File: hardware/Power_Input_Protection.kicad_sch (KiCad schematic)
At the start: 25 parts, among them J1 JST-PH, Q1 AO3401A, U1 TPS562202S, U2 TPS562202S

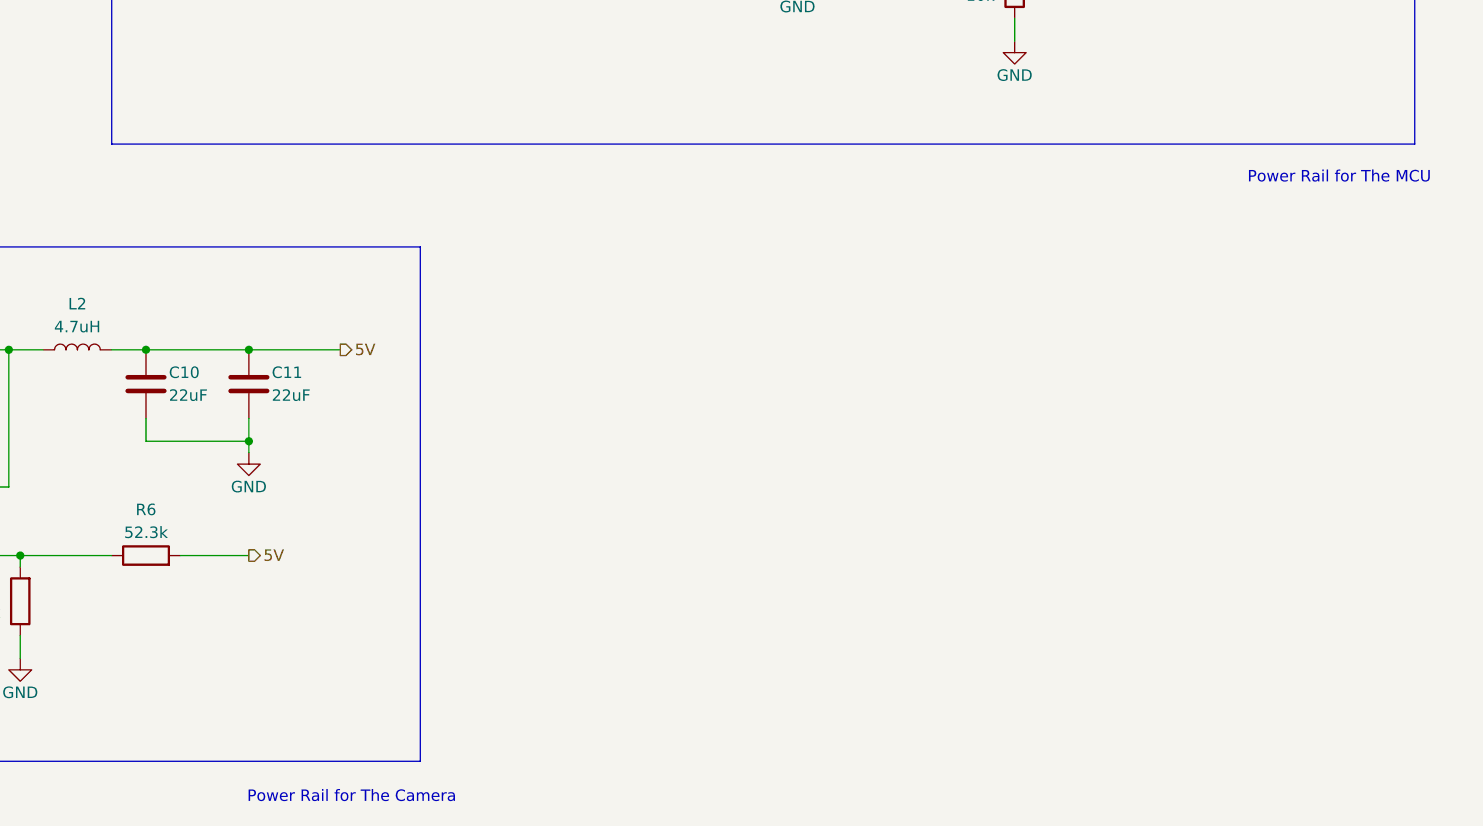
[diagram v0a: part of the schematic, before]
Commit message: Schematic for the MCU and Tag Connect
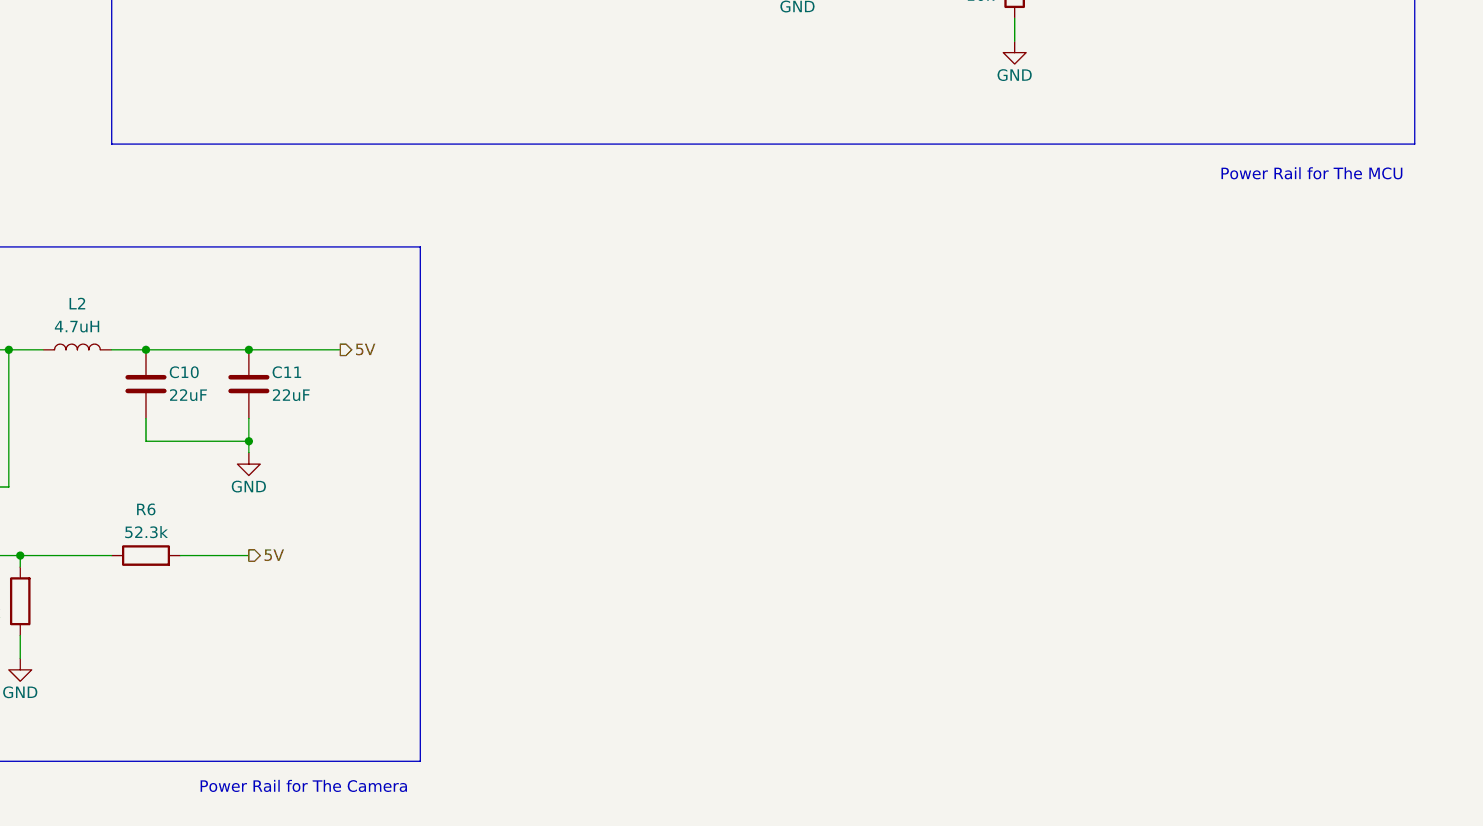
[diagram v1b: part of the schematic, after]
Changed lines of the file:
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@@
 	(text "Power Rail for The Camera\n"
 		(exclude_from_sim no)
-		(at 158.75 181.864 0)
+		(at 153.416 180.848 0)
 		(effects
 			(font
@@
 	(text "Power Rail for The MCU\n"
 		(exclude_from_sim no)
-		(at 268.478 113.03 0)
+		(at 265.43 112.776 0)
 		(effects
 			(font

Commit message: Completed Schematic
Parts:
- added C1: 47uF, symbol Device:C
- renumbered C6 to C10, C12 to C11, C10 to C12, C11 to C13, C1 to C2, C2 to C3, C3 to C4, C7 to C5, C8 to C6, C9 to C7, C4 to C8, C5 to C9, R6 to R4
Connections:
- net GND: now also C1.2
- net VBAT_RAW: now also C1.1
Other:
- moved on the sheet: J1

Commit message: Assigned Footprints and Libraries
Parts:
- C1: footprint (none) -> Capacitor_SMD:C_1210_3225Metric
- C10, C11, C4, C5: footprint (none) -> Capacitor_SMD:C_0603_1608Metric
- C12, C13, C6, C7: footprint (none) -> Capacitor_SMD:C_1206_3216Metric
- C2, C3, C8, C9: footprint (none) -> Capacitor_SMD:C_0805_2012Metric
- F1: footprint (none) -> PMHC_Footprints:F_1812_4532Metric
- J1: footprint (none) -> Connector_JST:JST_PH_S2B-PH-SM4-TB_1x02-1MP_P2.00mm_Horizontal
- L1: footprint (none) -> Inductor_SMD:L_Coilcraft_XFL2010
- L2: footprint (none) -> Inductor_SMD:L_Coilcraft_XAL4020-XXX
- R1, R2, R3, R4, R5: footprint (none) -> Resistor_SMD:R_0201_0603Metric
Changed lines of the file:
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@@
 			)
 		)
-		(property "Footprint" ""
+		(property "Footprint" "Resistor_SMD:R_0201_0603Metric"
 			(at 189.23 89.408 90)
 			(hide yes)
@@
 			)
 		)
-		(property "Footprint" ""
+		(property "Footprint" "Capacitor_SMD:C_1206_3216Metric"
 			(at 148.2852 139.7 0)
 			(hide yes)
@@
 			)
 		)
-		(property "Footprint" ""
+		(property "Footprint" "Capacitor_SMD:C_0805_2012Metric"
 			(at 49.2252 144.78 0)
 			(hide yes)
@@
 			)
 		)
-		(property "Footprint" ""
+		(property "Footprint" "Resistor_SMD:R_0201_0603Metric"
 			(at 234.188 91.44 90)
 			(hide yes)
@@
 			)
 		)
-		(property "Footprint" ""
+		(property "Footprint" "Capacitor_SMD:C_1210_3225Metric"
 			(at 44.1452 53.34 0)
 			(hide yes)
@@
 			)
 		)
-		(property "Footprint" ""
+		(property "Footprint" "Capacitor_SMD:C_1206_3216Metric"
 			(at 136.8552 139.7 0)
 			(hide yes)
@@
 			)
 		)
-		(property "Footprint" ""
+		(property "Footprint" "Capacitor_SMD:C_0805_2012Metric"
 			(at 171.1452 76.2 0)
 			(hide yes)
@@
 			)
 		)
-		(property "Footprint" ""
+		(property "Footprint" "Resistor_SMD:R_0201_0603Metric"
 			(at 135.89 156.718 90)
 			(hide yes)
@@
 			)
 		)
-		(property "Footprint" ""
+		(property "Footprint" "PMHC_Footprints:F_1812_4532Metric"
 			(at 58.42 43.18 0)
 			(hide yes)
@@
 			)
 		)
-		(property "Footprint" ""
+		(property "Footprint" "Resistor_SMD:R_0201_0603Metric"
 			(at 246.38 88.138 90)
 			(hide yes)
@@
 			)
 		)
-		(property "Footprint" ""
+		(property "Footprint" "Resistor_SMD:R_0201_0603Metric"
 			(at 123.698 160.02 90)
 			(hide yes)
@@
 			)
 		)
-		(property "Footprint" ""
+		(property "Footprint" "Inductor_SMD:L_Coilcraft_XFL2010"
 			(at 238.76 63.5 0)
 			(hide yes)
@@
 			)
 		)
-		(property "Footprint" ""
+		(property "Footprint" "Capacitor_SMD:C_1206_3216Metric"
 			(at 258.7752 71.12 0)
 			(hide yes)
@@
 			)
 		)
-		(property "Footprint" ""
+		(property "Footprint" "Capacitor_SMD:C_0603_1608Metric"
 			(at 228.6 77.7748 0)
 			(hide yes)
@@
 			)
 		)
-		(property "Footprint" ""
+		(property "Footprint" "Inductor_SMD:L_Coilcraft_XAL4020-XXX"
 			(at 128.27 132.08 0)
 			(hide yes)
@@
 			)
 		)
-		(property "Footprint" ""
+		(property "Footprint" "Capacitor_SMD:C_0603_1608Metric"
 			(at 118.11 146.3548 0)
 			(hide yes)
@@
 			)
 		)
-		(property "Footprint" ""
+		(property "Footprint" "Capacitor_SMD:C_0603_1608Metric"
 			(at 73.3552 144.78 0)
 			(hide yes)
@@
 			)
 		)
-		(property "Footprint" ""
+		(property "Footprint" "Connector_JST:JST_PH_S2B-PH-SM4-TB_1x02-1MP_P2.00mm_Horizontal"
 			(at 33.02 48.26 0)
 			(hide yes)
@@
 			)
 		)
-		(property "Footprint" ""
+		(property "Footprint" "Capacitor_SMD:C_0603_1608Metric"
 			(at 183.8452 76.2 0)
 			(hide yes)
@@
 			)
 		)
-		(property "Footprint" ""
+		(property "Footprint" "Capacitor_SMD:C_0805_2012Metric"
 			(at 159.7152 76.2 0)
 			(hide yes)
@@
 			)
 		)
-		(property "Footprint" ""
+		(property "Footprint" "Capacitor_SMD:C_0805_2012Metric"
 			(at 60.6552 144.78 0)
 			(hide yes)
@@
 			)
 		)
-		(property "Footprint" ""
+		(property "Footprint" "Capacitor_SMD:C_1206_3216Metric"
 			(at 247.3452 71.12 0)
 			(hide yes)

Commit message: Completed PCB Layout
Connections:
- net VBAT_PROT: now also C1.1; no longer D1.1 (A1)
- net VBAT_RAW: now also D1.1 (A1); no longer C1.1
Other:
- moved on the sheet: F1, Q1

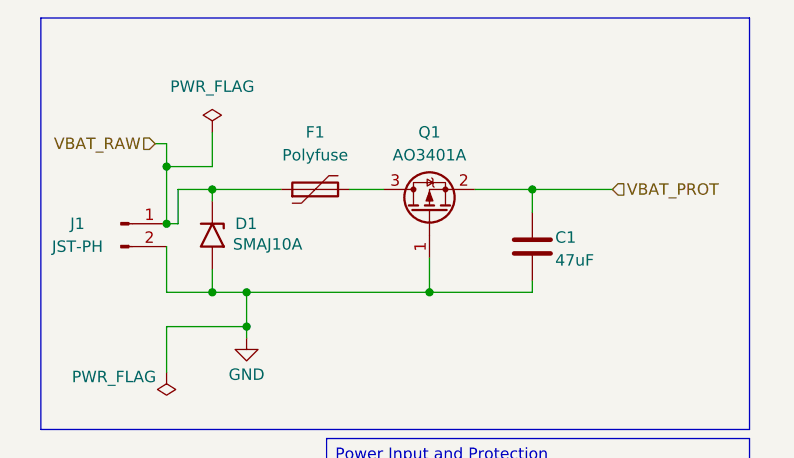
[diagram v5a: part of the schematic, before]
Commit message: PCB V1.1
Board completed, updated with labels for external connectors. Corrected and tightened hot loop with better layout and routing
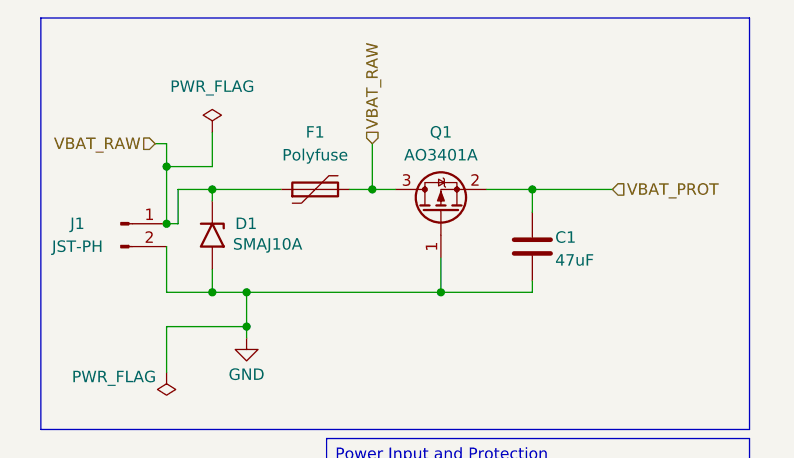
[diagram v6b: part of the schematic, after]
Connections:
- net VBAT_RAW: now also F1.2, Q1.3 (D)
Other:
- moved on the sheet: Q1
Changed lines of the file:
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@@
+	)
+	(junction
+		(at 60.96 44.45)
+		(diameter 0)
+		(color 0 0 0 0)
 	)
 	(junction
@@
 	)
 	(junction
-		(at 67.31 55.88)
-		(diameter 0)
-		(color 0 0 0 0)
-	)
-	(junction
 		(at 38.1 41.91)
 		(diameter 0)
@@
 	)
 	(junction
+		(at 43.18 55.88)
+		(diameter 0)
+		(color 0 0 0 0)
+	)
+	(junction
+		(at 59.69 132.08)
+		(diameter 0)
+		(color 0 0 0 0)
+	)
+	(junction
+		(at 135.89 132.08)
+		(diameter 0)
+		(color 0 0 0 0)
+	)
+	(junction
+		(at 257.81 63.5)
+		(diameter 0)
+		(color 0 0 0 0)
+	)
+	(junction
+		(at 182.88 63.5)
+		(diameter 0)
+		(color 0 0 0 0)
+	)
+	(junction
 		(at 78.74 44.45)
 		(diameter 0)
@@
 	)
 	(junction
-		(at 43.18 55.88)
-		(diameter 0)
-		(color 0 0 0 0)
-	)
-	(junction
-		(at 59.69 132.08)
-		(diameter 0)
-		(color 0 0 0 0)
-	)
-	(junction
-		(at 135.89 132.08)
-		(diameter 0)
-		(color 0 0 0 0)
-	)
-	(junction
-		(at 257.81 63.5)
-		(diameter 0)
-		(color 0 0 0 0)
-	)
-	(junction
-		(at 182.88 63.5)
-		(diameter 0)
-		(color 0 0 0 0)
-	)
-	(junction
 		(at 232.41 86.36)
 		(diameter 0)
@@
 	)
 	(junction
+		(at 68.58 55.88)
+		(diameter 0)
+		(color 0 0 0 0)
+	)
+	(junction
 		(at 59.69 147.32)
 		(diameter 0)
@@
 	(wire
 		(pts
-			(xy 46.99 55.88) (xy 67.31 55.88)
+			(xy 46.99 55.88) (xy 68.58 55.88)
 		)
 		(stroke
@@
 	(wire
 		(pts
-			(xy 58.42 44.45) (xy 62.23 44.45)
+			(xy 58.42 44.45) (xy 60.96 44.45)
 		)
 		(stroke
@@
 	(wire
 		(pts
-			(xy 78.74 55.88) (xy 67.31 55.88)
+			(xy 78.74 55.88) (xy 68.58 55.88)
 		)
 		(stroke
@@
 	(wire
 		(pts
-			(xy 67.31 52.07) (xy 67.31 55.88)
+			(xy 68.58 52.07) (xy 68.58 55.88)
 		)
 		(stroke
@@
 	(wire
 		(pts
+			(xy 60.96 39.37) (xy 60.96 44.45)
+		)
+		(stroke
+			(width 0)
+			(type default)
+		)
+	)
+	(wire
+		(pts
 			(xy 121.92 163.83) (xy 121.92 166.37)
 		)
@@
 	(wire
 		(pts
+			(xy 60.96 44.45) (xy 63.5 44.45)
+		)
+		(stroke
+			(width 0)
+			(type default)
+		)
+	)
+	(wire
+		(pts
 			(xy 231.14 63.5) (xy 234.95 63.5)
 		)
@@
 	(wire
 		(pts
-			(xy 72.39 44.45) (xy 78.74 44.45)
+			(xy 73.66 44.45) (xy 78.74 44.45)
 		)
 		(stroke
@@
 		(shape output)
 		(at 267.97 63.5 0)
+		(effects
+			(font
+				(size 1.27 1.27)
+			)
+			(justify left)
+		)
+	)
+	(hierarchical_label "VBAT_RAW"
+		(shape input)
+		(at 60.96 39.37 90)
 		(effects
 			(font
@@
 	(symbol
 		(lib_id "Transistor_FET:AO3401A")
-		(at 67.31 46.99 90)
+		(at 68.58 46.99 90)
 		(unit 1)
 		(body_style 1)
@@
 		(fields_autoplaced yes)
 		(property "Reference" "Q1"
-			(at 67.31 38.1 90)
+			(at 68.58 38.1 90)
 			(show_name no)
 			(do_not_autoplace no)
@@
 		)
 		(property "Value" "AO3401A"
-			(at 67.31 40.64 90)
+			(at 68.58 40.64 90)
 			(show_name no)
 			(do_not_autoplace no)
@@
 		)
 		(property "Footprint" "Package_TO_SOT_SMD:SOT-23"
-			(at 69.215 41.91 0)
+			(at 70.485 41.91 0)
 			(hide yes)
 			(show_name no)
@@
 		)
 		(property "Datasheet" "http://www.aosmd.com/pdfs/datasheet/AO3401A.pdf"
-			(at 71.12 41.91 0)
+			(at 72.39 41.91 0)
 			(hide yes)
 			(show_name no)
@@
 		)
 		(property "Description" "-4.0A Id, -30V Vds, P-Channel MOSFET, SOT-23"
-			(at 67.31 46.99 0)
-			(hide yes)
-			(show_name no)
+			(at 68.58 46.99 0)
+			(hide yes)
+			(show_name no)
